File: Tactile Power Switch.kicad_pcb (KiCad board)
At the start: 2 copper layers, 22 x 26 mm, 17 parts, among them J1 OSTTC020162, J2 OSTTC020162, Q1 BC847B_215, Q2 BC847B_215, Q4 NDT2955, SW1 SW_SPST

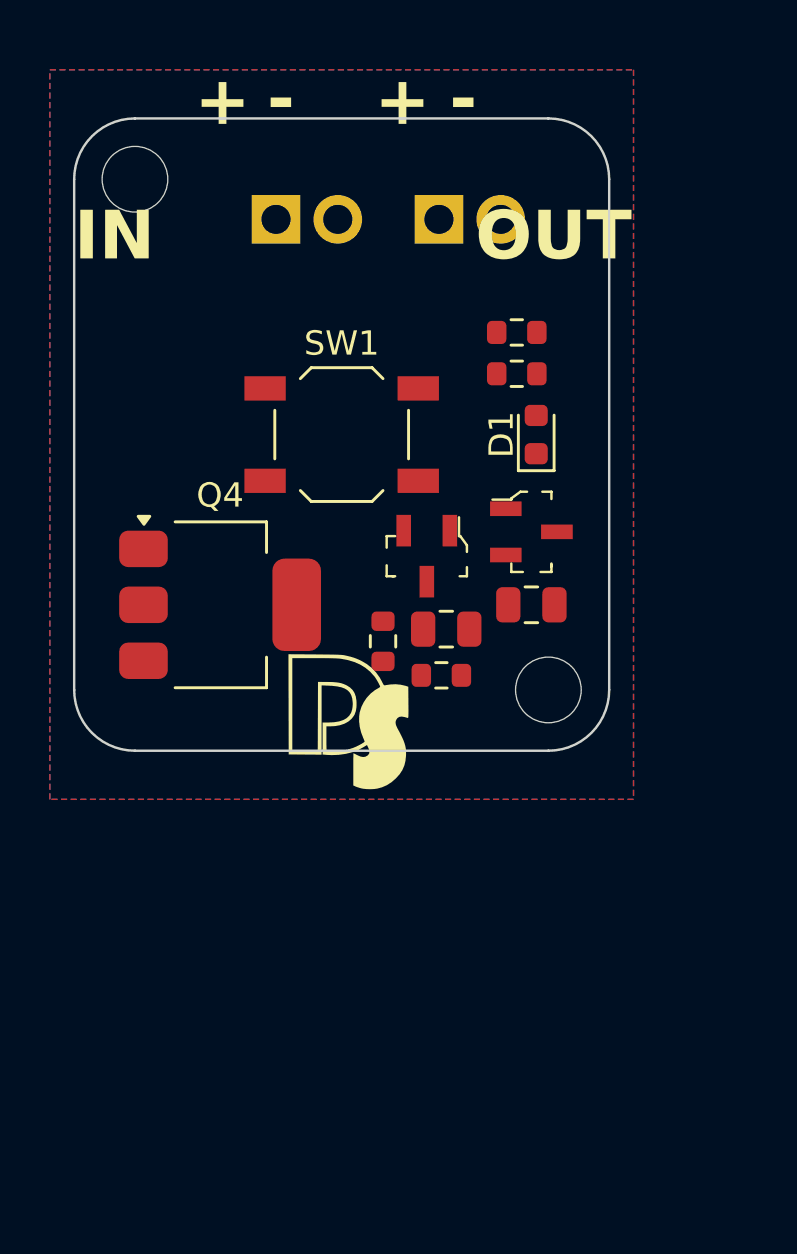
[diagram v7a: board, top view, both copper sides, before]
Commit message: Silkscreen added
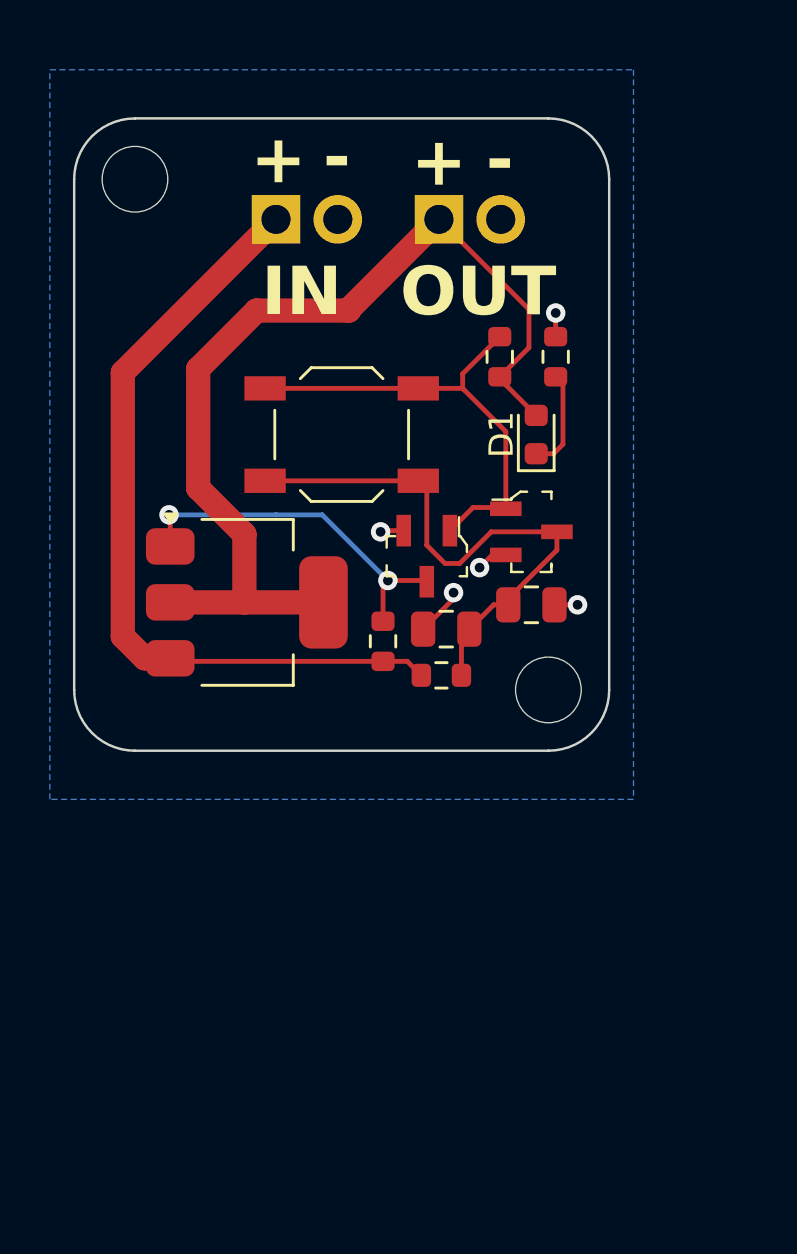
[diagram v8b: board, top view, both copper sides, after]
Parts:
- added REF**: OSHW-Symbol_6.7x6mm_SilkScreen, Symbol:OSHW-Symbol_6.7x6mm_SilkScreen, B.Cu at (114.1, 68.3)
- G***: moved to B.Cu
- moved G*** 9.01 mm to (111.5, 62.0)
- moved G*** 3.19 mm to (122.4, 68.4), turned to 180 degrees
- moved R4 1.89 mm to (128.8, 55.8), turned to 90 degrees
- moved Q4 1.10 mm to (116.1, 65.9)
- moved R2 0.99 mm to (126.5, 55.8), turned to 90 degrees
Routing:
- net VDD: track 0.00 -> 39.9 mm
- net +12V: track 0.00 -> 32.7 mm
- net Net-(Q2-C): track 0.00 -> 23.2 mm
- net Net-(Q1-B): track 0.00 -> 19.3 mm
- net Net-(Q1-C): track 0.00 -> 14.8 mm, vias 0 -> 2
- net GND: track 0.00 -> 6.21 mm, vias 0 -> 5
- net Net-(D1-K): track 0.00 -> 4.16 mm
- removed copper zone on F.Cu, net GND
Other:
- board text added: "SMD VERSION REV.01"
- board text added: "Tactile ON/OFF Power Button"
